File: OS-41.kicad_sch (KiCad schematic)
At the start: 70 parts, among them J1 Conn_01x02_Pin, J2 Conn_01x02_Pin, J3 Conn_01x02_Pin, J4 Conn_Coaxial, J5 Conn_01x02_Pin, J6 Conn_01x04_Pin, J7 Conn_01x09_Pin, J8 Conn_01x02_Pin, J9 Conn_01x02_Pin, U1 GPS1003, U2 SI4432-B1-FMR, U3 MCP1640x-xCHY, U4 ATGM336H-5N31, U5 DS18B20, U6 BMP390L, U7 STM32F411CEUx, X1 SMD-3225_4P 30.000MHZ 10PF, Y1 Crystal_GND24, Y2 Crystal

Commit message: Progress
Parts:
- removed J1, J5: Conn_01x02_Pin, Connector_PinSocket_2.54mm:PinSocket_1x02_P2.54mm_Vertical, symbol Connector:Conn_01x02_Pin
- removed J7: Conn_01x09_Pin, Connector_PinSocket_2.54mm:PinSocket_1x09_P2.54mm_Vertical, symbol Connector:Conn_01x09_Pin
- removed U1: GPS1003, libsos41:ANT-SMD_L10.0-W3.0, symbol libs:GPS1003
- removed X1: SMD-3225_4P 30.000MHZ 10PF, libsos41:CRYSTAL-SMD_4P-L3.2-W2.5-BL, symbol crystal:SMD-3225_4P30.000MHZ10PF
- added AE1: Antenna, libsos41:ANT-SMD_L10.0-W3.0, symbol Device:Antenna
- added Y3: Crystal_GND24, Crystal:Crystal_SMD_3225-4Pin_3.2x2.5mm, symbol Device:Crystal_GND24
- C15, C17, C18, C19, C20, C21, C22, C23, C24, C25, C26: footprint (none) -> Capacitor_SMD:C_0603_1608Metric_Pad1.08x0.95mm_HandSolder
- J2, J3: footprint Connector_PinSocket_2.54mm:PinSocket_1x02_P2.54mm_Vertical -> Connector_PinHeader_2.54mm:PinHeader_1x02_P2.54mm_Vertical
- J6: footprint (none) -> Connector_PinHeader_2.54mm:PinHeader_1x04_P2.54mm_Vertical
- J8, J9: footprint (none) -> Connector_PinHeader_2.54mm:PinHeader_1x02_P2.54mm_Vertical
- L7: footprint (none) -> Inductor_SMD:L_0603_1608Metric_Pad1.05x0.95mm_HandSolder
- R5, R6, R7: footprint (none) -> Resistor_SMD:R_0603_1608Metric_Pad0.98x0.95mm_HandSolder
- U2: footprint libsos41:QLP20 -> centdir:QFN50P400X400X90-21N
- Y1: footprint Crystal:Crystal_SMD_3225-4Pin_3.2x2.5mm_HandSoldering -> Crystal:Crystal_SMD_3225-4Pin_3.2x2.5mm
- Y2: footprint (none) -> Crystal:Crystal_SMD_2012-2Pin_2.0x1.2mm_HandSoldering
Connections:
- net GPIO2 is gone; now on net NIRQ: U7.25 (PB12)
- net GPIO3 is gone; now on net SDN: U7.26 (PB13)
- net GND: now also Y3.2, Y3.4
- net GPS_ANT: now also AE1.1 (A)
- net at U2.19 (XIN): now also Y3.1
- net at U2.18 (XOUT): now also Y3.3
- no-connect marks 17 -> 18
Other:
- note removed: "General-purpose GPIOs for interfacing"

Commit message: Preliminary board
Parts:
- added C27: 100nF, Capacitor_SMD:C_0603_1608Metric_Pad1.08x0.95mm_HandSolder, symbol Device:C
- added C28: 10uF, Capacitor_SMD:C_0603_1608Metric_Pad1.08x0.95mm_HandSolder, symbol Device:C
- Y2: footprint Crystal:Crystal_SMD_2012-2Pin_2.0x1.2mm_HandSoldering -> Crystal:Crystal_SMD_3215-2Pin_3.2x1.5mm
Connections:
- net GND: now also C27.2, C28.2
- net VCC: now also C27.1, C28.1
- no-connect marks 18 -> 26

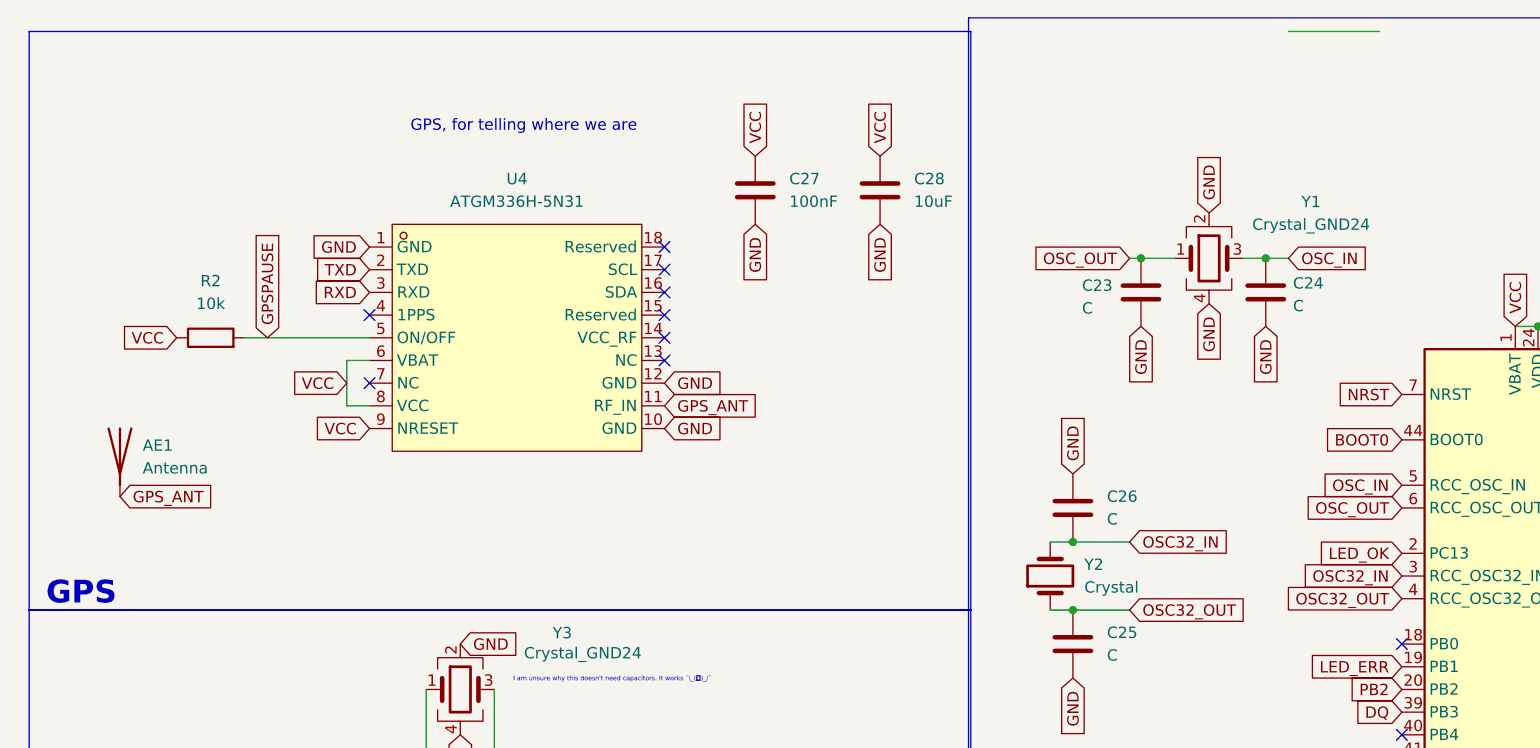
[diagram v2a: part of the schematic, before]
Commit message: Change GPS antenna + routing fixes
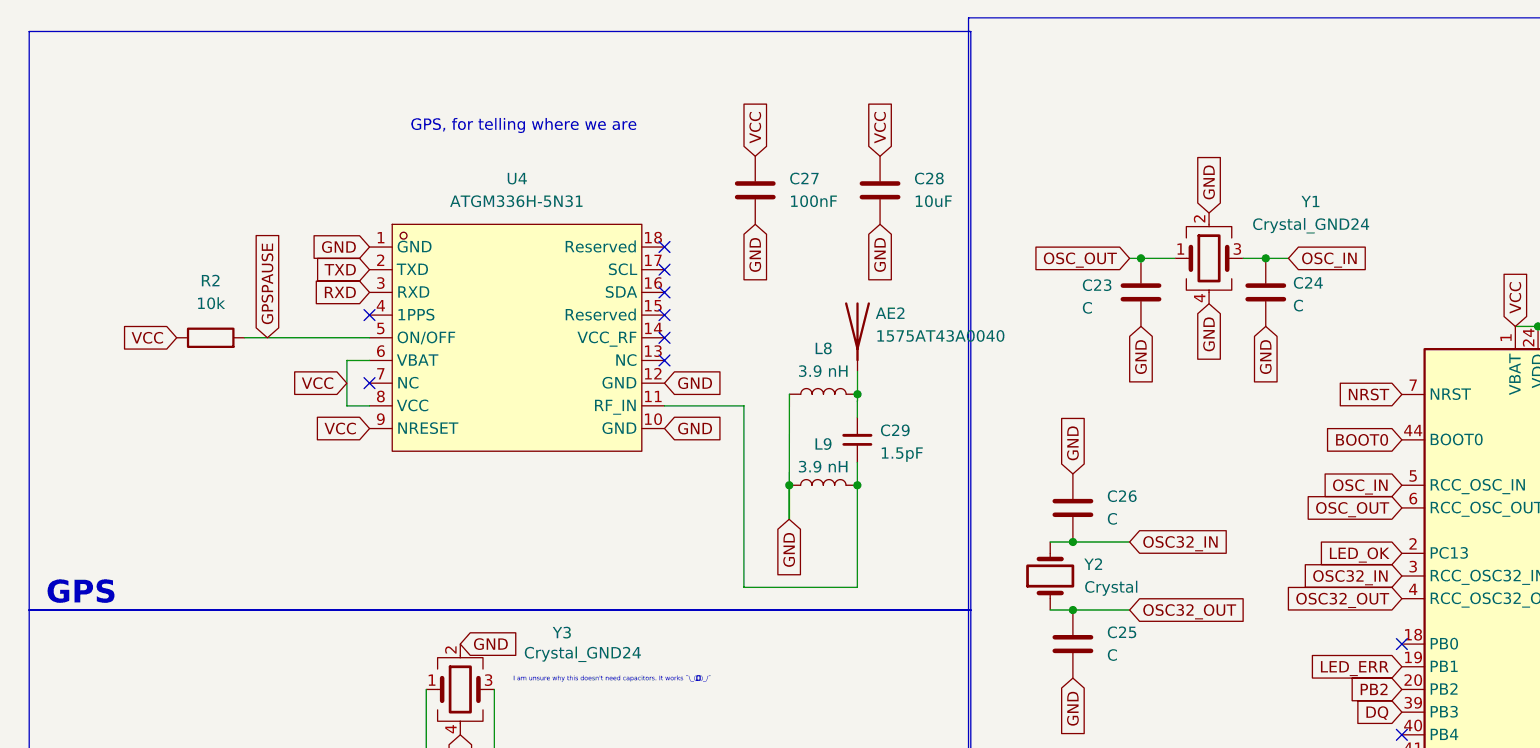
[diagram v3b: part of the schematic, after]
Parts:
- removed AE1: Antenna, libsos41:ANT-SMD_L10.0-W3.0, symbol Device:Antenna
- added AE2: 1575AT43A0040, centdir:ANT_1575AT_JOT, symbol Device:Antenna
- added C29: 1.5pF, Capacitor_SMD:C_0402_1005Metric_Pad0.74x0.62mm_HandSolder, symbol Device:C_Small
- added L8, L9: 3.9 nH, Inductor_SMD:L_0402_1005Metric_Pad0.77x0.64mm_HandSolder, symbol Device:L
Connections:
- net GND: now also L8.1, L9.1
- net GPS_ANT: no longer names the net of U4.11 (RF_IN)
- net GPS_ANT: now also C29.1, L9.2
- new net: AE2.1 (A), C29.2, L8.2

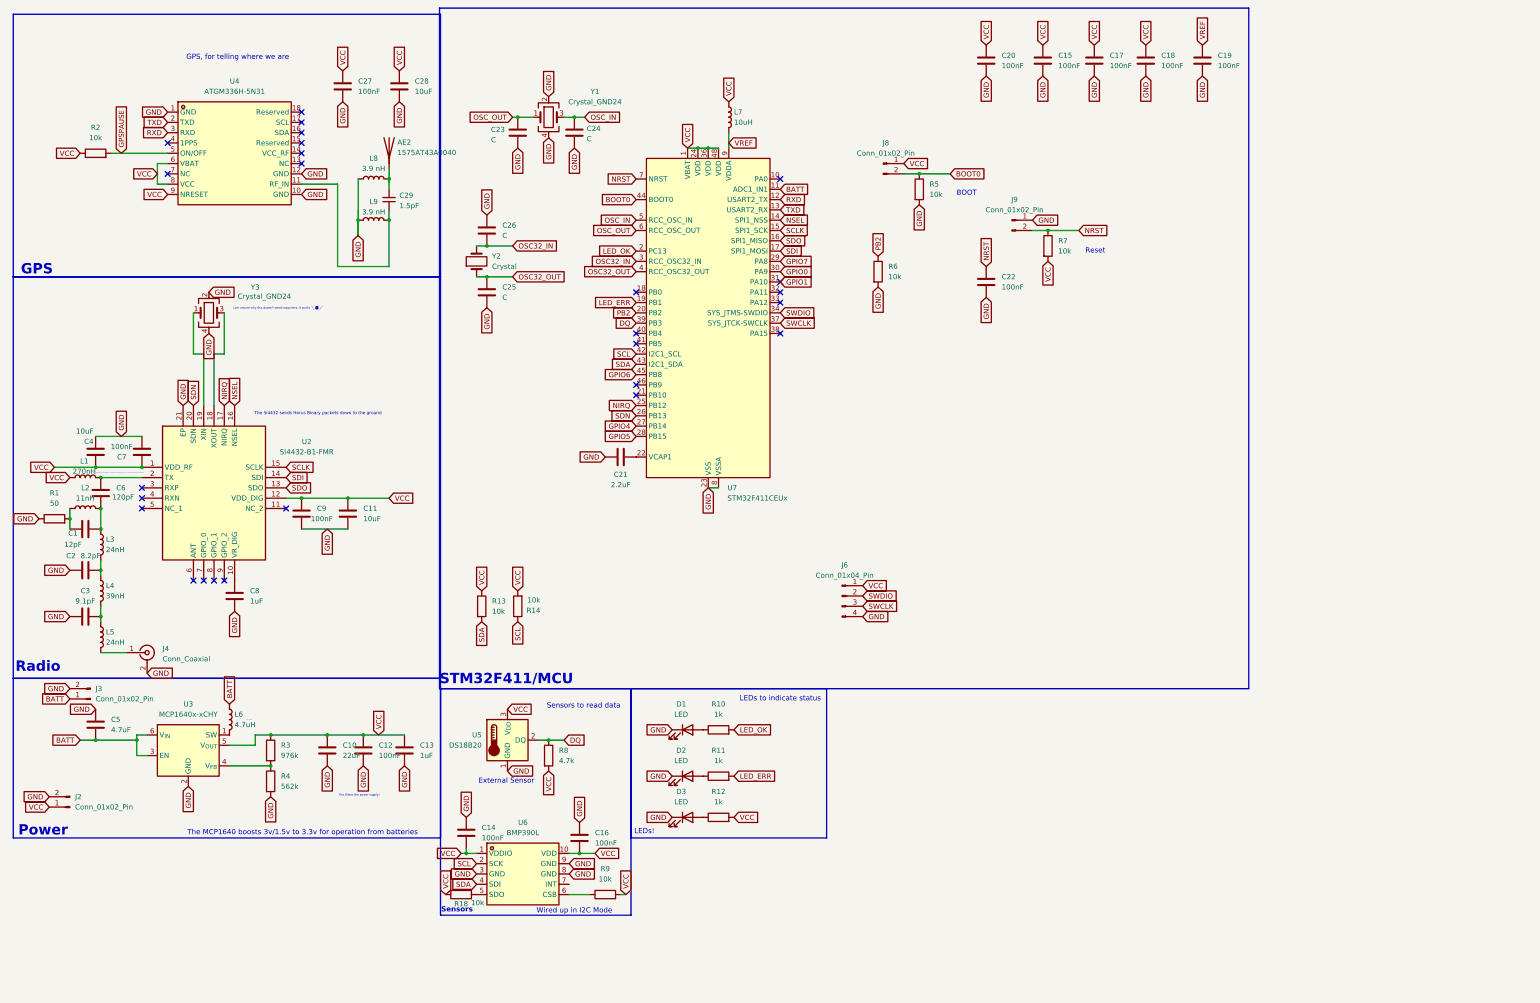
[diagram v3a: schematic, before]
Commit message: Remaking the PCB... again...
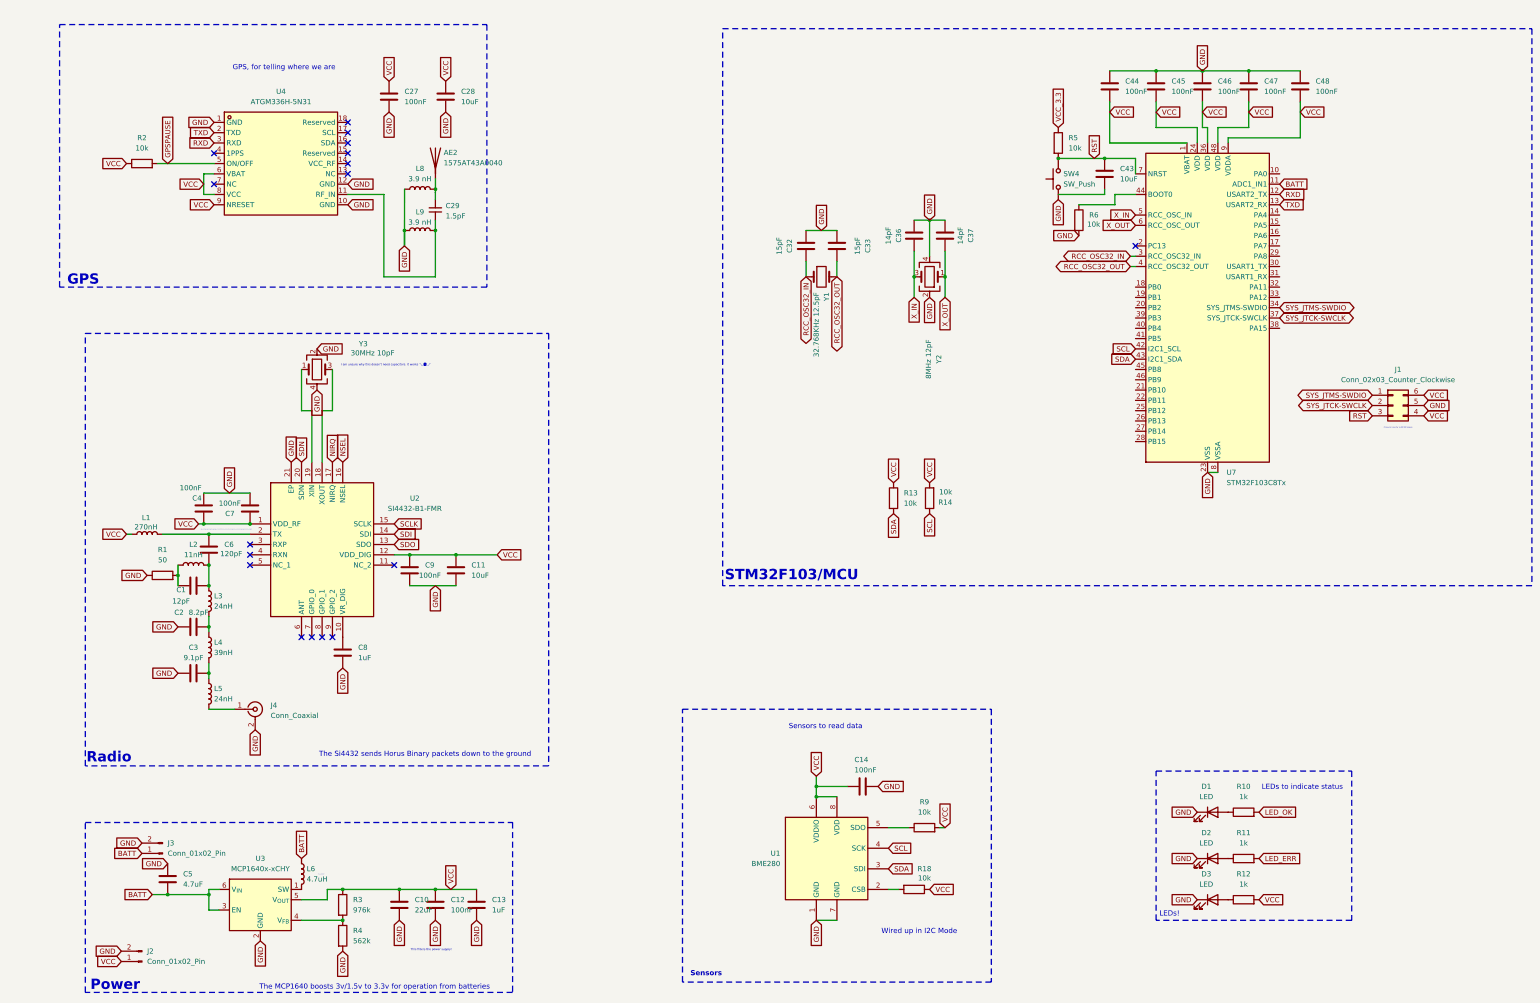
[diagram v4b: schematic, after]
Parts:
- removed C15, C16, C17, C18, C19, C20, C22: 100nF, Capacitor_SMD:C_0603_1608Metric_Pad1.08x0.95mm_HandSolder, symbol Device:C
- removed C21: 2.2uF, Capacitor_SMD:C_0603_1608Metric_Pad1.08x0.95mm_HandSolder, symbol Device:C
- removed C23, C24, C25, C26: C, Capacitor_SMD:C_0603_1608Metric_Pad1.08x0.95mm_HandSolder, symbol Device:C
- removed J6: Conn_01x04_Pin, Connector_PinHeader_2.54mm:PinHeader_1x04_P2.54mm_Vertical, symbol Connector:Conn_01x04_Pin
- removed J8, J9: Conn_01x02_Pin, Connector_PinHeader_2.54mm:PinHeader_1x02_P2.54mm_Vertical, symbol Connector:Conn_01x02_Pin
- removed L7: 10uH, Inductor_SMD:L_0603_1608Metric_Pad1.05x0.95mm_HandSolder, symbol Device:L
- removed R7: 10k, Resistor_SMD:R_0603_1608Metric_Pad0.98x0.95mm_HandSolder, symbol Device:R
- removed R8: 4.7k, Resistor_SMD:R_0603_1608Metric_Pad0.98x0.95mm_HandSolder, symbol Device:R
- removed U5: DS18B20, Package_TO_SOT_THT:TO-92_Inline, symbol Sensor_Temperature:DS18B20
- removed U6: BMP390L, libsos41:LGA-10_L2.0-W2.0-P0.50-TL_BMP390L, symbol libs:BMP390L
- removed U7: STM32F411CEUx, Package_DFN_QFN:QFN-48-1EP_7x7mm_P0.5mm_EP5.6x5.6mm, symbol MCU_ST_STM32F4:STM32F411CEUx
- removed Y1: Crystal_GND24, Crystal:Crystal_SMD_3225-4Pin_3.2x2.5mm, symbol Device:Crystal_GND24
- removed Y2: Crystal, Crystal:Crystal_SMD_3215-2Pin_3.2x1.5mm, symbol Device:Crystal
- added C32, C33: 15pF, Capacitor_SMD:C_0603_1608Metric_Pad1.08x0.95mm_HandSolder, symbol Device:C
- added C36, C37: 14pF, Capacitor_SMD:C_0603_1608Metric_Pad1.08x0.95mm_HandSolder, symbol Device:C
- added C43: 10uF, Capacitor_SMD:C_0603_1608Metric_Pad1.08x0.95mm_HandSolder, symbol Device:C
- added C44, C45, C46, C47, C48: 100nF, Capacitor_SMD:C_0603_1608Metric_Pad1.08x0.95mm_HandSolder, symbol Device:C
- added J1: Conn_02x03_Counter_Clockwise, Connector_PinHeader_2.54mm:PinHeader_2x03_P2.54mm_Vertical, symbol Connector_Generic:Conn_02x03_Counter_Clockwise
- added SW4: SW_Push, Button_Switch_THT:SW_PUSH_6mm, symbol Switch:SW_Push
- added U1: BME280, Package_LGA:Bosch_LGA-8_2.5x2.5mm_P0.65mm_ClockwisePinNumbering, symbol Sensor:BME280
- added U7: STM32F103C8Tx, Package_QFP:LQFP-48_7x7mm_P0.5mm, symbol MCU_ST_STM32F1:STM32F103C8Tx
- added Y1: 32.768KHz 12.5pF, Crystal:Crystal_SMD_3215-2Pin_3.2x1.5mm, symbol Device:Crystal
- added Y2: 8MHz 12pF, Crystal:Crystal_SMD_3225-4Pin_3.2x2.5mm, symbol Device:Crystal_GND24
- C4: value 10uF -> 100nF
- Y3: value Crystal_GND24 -> 30MHz 10pF
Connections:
- net BATT: now also U7.11 (PA1)
- net GND: now also C32.1, C33.1, C36.1, C37.1, C44.1, C45.1, C46.1, C47.1, C48.1, J1.5 (Pin_5), SW4.1, U1.1 (GND), U1.7 (GND), U7.23 (VSS), U7.35 (VSS), U7.47 (VSS), U7.8 (VSSA), Y2.2, Y2.4; no longer R5.2
- net RXD: now also U7.12 (PA2)
- net SCL: now also U1.4 (SCK), U7.42 (PB6)
- net SDA: now also U1.3 (SDI), U7.43 (PB7)
- net TXD: now also U7.13 (PA3)
- net VCC: now also C44.2, C45.2, C46.2, C47.2, C48.2, J1.4 (Pin_4), J1.6 (Pin_6), U1.6 (VDDIO), U1.8 (VDD), U7.1 (VBAT), U7.24 (VDD), U7.36 (VDD), U7.48 (VDD), U7.9 (VDDA)
- net at R18.2: now also U1.2 (CSB)
- net at R9.1: now also U1.5 (SDO)
- net BOOT0 renamed VCC_3.3
- net PB2: no longer names the net of R6.1
- net PB2: now also U7.44 (BOOT0)
- new net RCC_OSC32_IN: C32.2, U7.3 (PC14), Y1.1
- new net RCC_OSC32_OUT: C33.2, U7.4 (PC15), Y1.2
- new net RST: C43.1, J1.3 (Pin_3), R5.2, SW4.2, U7.7 (NRST)
- new net SYS_JTCK-SWCLK: J1.2 (Pin_2), U7.37 (PA14)
- new net SYS_JTMS-SWDIO: J1.1 (Pin_1), U7.34 (PA13)
- new net X_IN: C36.2, U7.5 (PD0), Y2.3
- new net X_OUT: C37.2, U7.6 (PD1), Y2.1
- no-connect marks 26 -> 17
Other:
- note added: "Oh boy do I love the 'ol AVR ISP headers"
- note added: "STM32F103/MCU"
- note removed: "BOOT"
- note removed: "External Sensor"
- note removed: "Reset"
- note removed: "STM32F411/MCU"
- moved on the sheet: AE2, C1, C10, C11, C12, C13, C14, C2, C27, C28, C29, C3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

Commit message: Continue layout
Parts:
- SW4: footprint Button_Switch_THT:SW_PUSH_6mm -> libsos41:SMD_SW_NEW_REDONE
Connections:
- net NIRQ: now also U7.29 (PA8)
- net NSEL: now also U7.14 (PA4)
- net SCLK: now also U7.15 (PA5)
- net SDI: now also U7.17 (PA7)
- net SDN: now also U7.30 (PA9)
- net SDO: now also U7.16 (PA6)
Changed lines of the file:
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@@
 		)
 	)
+	(global_label "NIRQ"
+		(shape input)
+		(at 326.39 76.2 0)
+		(effects
+			(font
+				(size 1.27 1.27)
+			)
+			(justify left)
+		)
+		(property "Intersheetrefs" "${INTERSHEET_REFS}"
+			(at 326.39 76.2 90)
+			(effects
+				(font
+					(size 1.27 1.27)
+				)
+				(hide yes)
+			)
+		)
+	)
+	(global_label "SDO"
+		(shape input)
+		(at 326.39 71.12 0)
+		(effects
+			(font
+				(size 1.27 1.27)
+			)
+			(justify left)
+		)
+		(property "Intersheetrefs" "${INTERSHEET_REFS}"
+			(at 326.39 71.12 0)
+			(effects
+				(font
+					(size 1.27 1.27)
+				)
+				(hide yes)
+			)
+		)
+	)
 	(global_label "VCC"
 		(shape input)
@@
 		)
 	)
+	(global_label "SDN"
+		(shape input)
+		(at 326.39 78.74 0)
+		(effects
+			(font
+				(size 1.27 1.27)
+			)
+			(justify left)
+		)
+		(property "Intersheetrefs" "${INTERSHEET_REFS}"
+			(at 326.39 78.74 90)
+			(effects
+				(font
+					(size 1.27 1.27)
+				)
+				(hide yes)
+			)
+		)
+	)
 	(global_label "RST"
 		(shape input)
@@
 		)
 	)
+	(global_label "SDI"
+		(shape input)
+		(at 326.39 73.66 0)
+		(effects
+			(font
+				(size 1.27 1.27)
+			)
+			(justify left)
+		)
+		(property "Intersheetrefs" "${INTERSHEET_REFS}"
+			(at 326.39 73.66 0)
+			(effects
+				(font
+					(size 1.27 1.27)
+				)
+				(hide yes)
+			)
+		)
+	)
 	(global_label "TXD"
 		(shape input)
@@
 		)
 	)
+	(global_label "SCLK"
+		(shape input)
+		(at 326.39 68.58 0)
+		(effects
+			(font
+				(size 1.27 1.27)
+			)
+			(justify left)
+		)
+		(property "Intersheetrefs" "${INTERSHEET_REFS}"
+			(at 326.39 68.58 0)
+			(effects
+				(font
+					(size 1.27 1.27)
+				)
+				(hide yes)
+			)
+		)
+	)
 	(global_label "GND"
 		(shape input)
@@
 		)
 	)
+	(global_label "NSEL"
+		(shape input)
+		(at 326.39 66.04 0)
+		(effects
+			(font
+				(size 1.27 1.27)
+			)
+			(justify left)
+		)
+		(property "Intersheetrefs" "${INTERSHEET_REFS}"
+			(at 326.39 66.04 90)
+			(effects
+				(font
+					(size 1.27 1.27)
+				)
+				(hide yes)
+			)
+		)
+	)
 	(global_label "GND"
 		(shape input)
@@
 			)
 		)
-		(property "Footprint" "Button_Switch_THT:SW_PUSH_6mm"
+		(property "Footprint" "libsos41:SMD_SW_NEW_REDONE"
 			(at 266.7 57.15 0)
 			(effects
@@
 		)
 		(pin "22"
+			(alternate "USART3_RX")
 		)
 		(pin "28"
@@
 		)
 		(pin "16"
+			(alternate "SPI1_MISO")
 		)
 		(pin "17"
+			(alternate "SPI1_MOSI")
 		)
 		(pin "32"
@@
 		)
 		(pin "15"
+			(alternate "SPI1_SCK")
 		)
 		(pin "13"
@@
 		)
 		(pin "31"
-			(alternate "USART1_RX")
 		)
 		(pin "26"
@@
 		)
 		(pin "30"
-			(alternate "USART1_TX")
 		)
 		(pin "48"
@@
 		)
 		(pin "14"
+			(alternate "SPI1_NSS")
 		)
 		(pin "21"
+			(alternate "USART3_TX")
 		)
 		(pin "23"
